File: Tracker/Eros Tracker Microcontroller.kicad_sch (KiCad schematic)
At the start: 20 parts, among them M1 Motor_DC, Q1 NX138BKSX, Q2 NX138BKSX, Q3 DMP31D7LDW-7, SW1 EVQ-P7A01P, U1 ESP32-C3-WROOM-02-N4

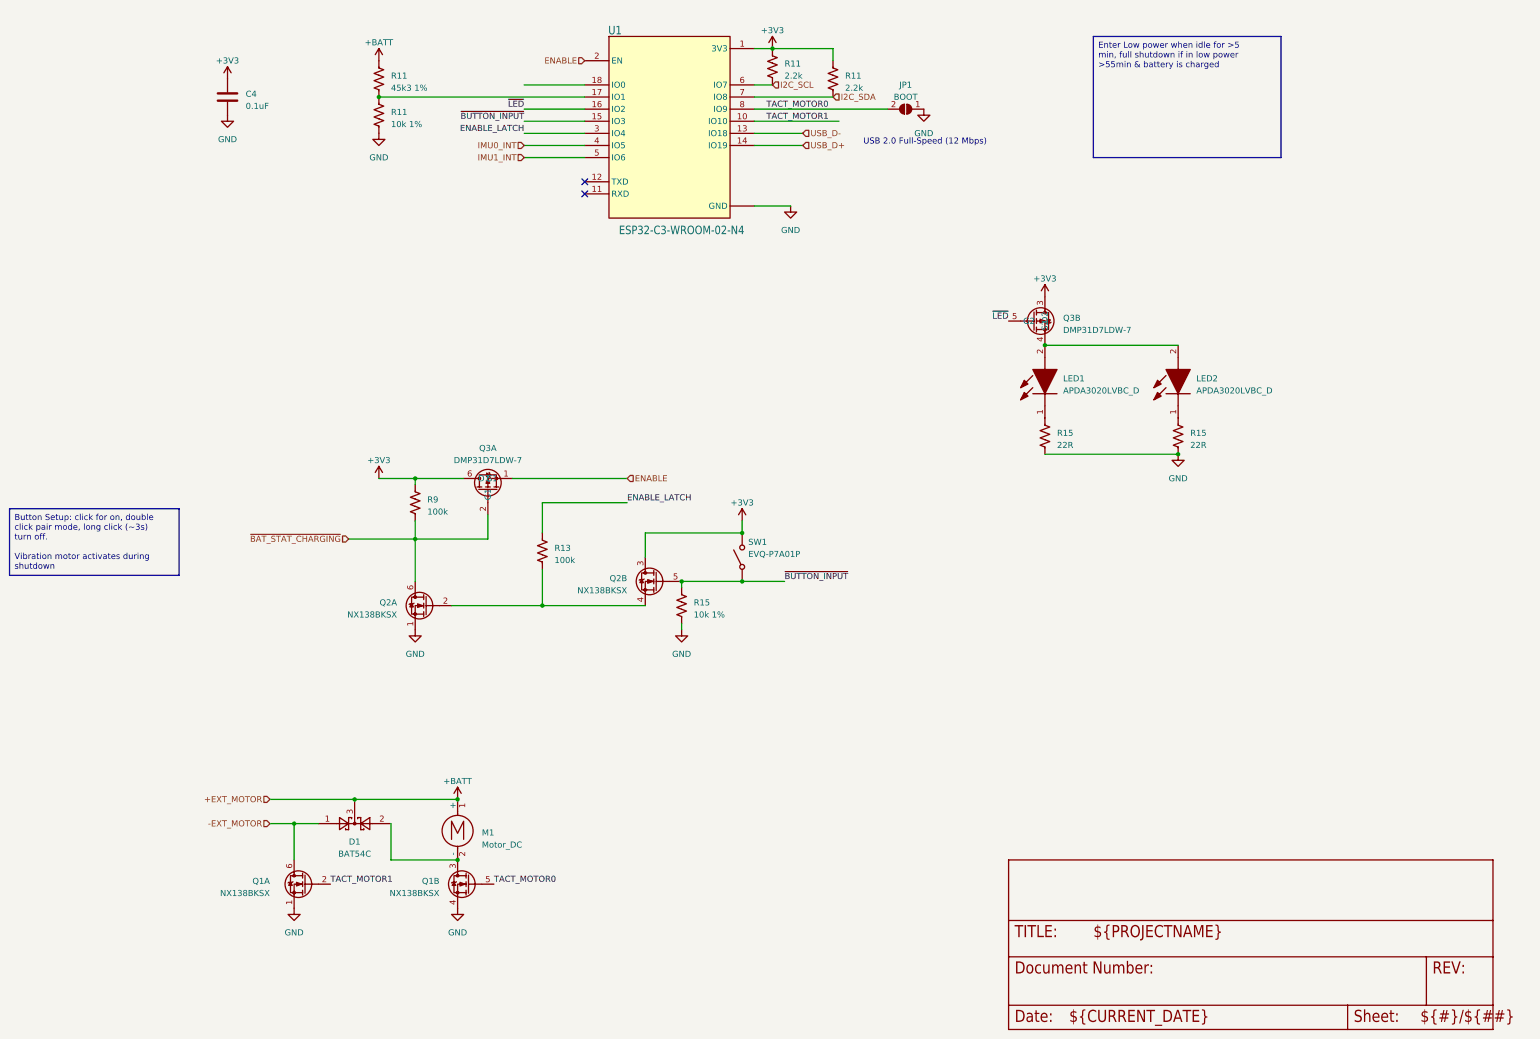
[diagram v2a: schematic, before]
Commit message: RevC release. Power passthrough, battery voltage monitoring, IMU interrupt line fixed. TVS diodes added to all human-reachable connections.
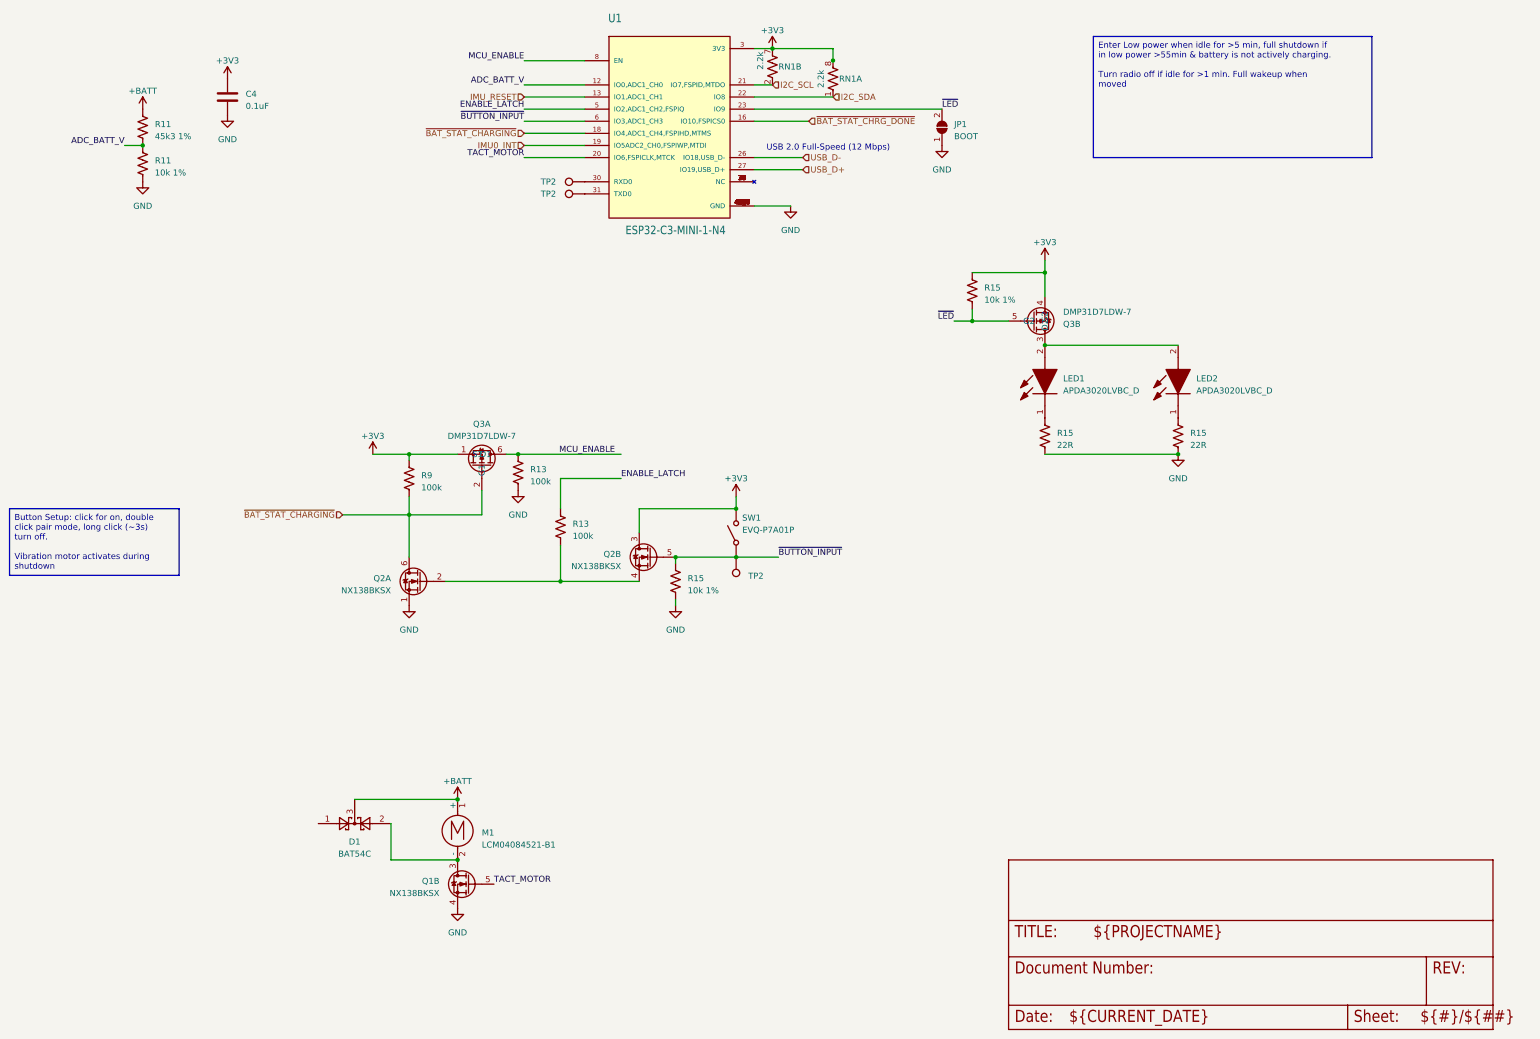
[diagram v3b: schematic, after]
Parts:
- removed unit 1 of Q1
- removed R11 (x2): 2.2k, Resistor_SMD:R_0805_2012Metric, symbol Device:R_US
- added R13: 100k, Resistor_SMD:R_0402_1005Metric, symbol Device:R_US
- added R15: 10k 1%, Resistor_SMD:R_0402_1005Metric, symbol Device:R_US
- added RN1: 2.2k, Eros Tracker:CAY10-xxxJ4, symbol Eros Tracker:CAY10-xxxJ4
- added TP2 (x3): TestPoint, TestPoint:TestPoint_Pad_D1.0mm, symbol Connector:TestPoint
- C4: footprint Capacitor_SMD:C_0805_2012Metric -> Capacitor_SMD:C_0402_1005Metric; Manufacturer_Part_Number CL21B104MACNNNC -> CL05B104KA5NNNC; Mouser Part Number 187-CL21B104MACNNNC -> 187-CL05B104KA5NNNC; Mouser Price/Stock https://www.mouser.com/ProductDetail/Samsung-Electro-Mechanics/CL21B104MACNNNC?qs=xZ%2FP%252Ba9zWqbIolF6La19LA%3D%3D -> https://www.mouser.com/ProductDetail/Samsung-Electro-Mechanics/CL05B104KA5NNNC?qs=Efv9o2T6U88DLyyMSzjXSQ%3D%3D
- LED1, LED2: footprint APDA3020LVBCD -> Eros Tracker:APDA3020LVBCD
- M1: value Motor_DC -> LCM04084521-B1; footprint Jumper:SolderJumper-2_P1.3mm_Open_RoundedPad1.0x1.5mm -> Eros Tracker:LCM04084521-B1
- Q3: footprint SOT65P210X110-6N -> Eros Tracker:SOT65P210X110-6N
- R11, R15: footprint Resistor_SMD:R_0805_2012Metric -> Resistor_SMD:R_0402_1005Metric; Manufacturer_Part_Number RT0805FRE0710KL -> RT0402FRE0710KL; Mouser Part Number 603-RT0805FRE0710KL -> 603-RT0402FRE0710KL; Mouser Price/Stock https://www.mouser.com/ProductDetail/YAGEO/RT0805FRE0710KL?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 -> https://www.mouser.com/ProductDetail/YAGEO/RT0402FRE0710KL?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
- R11: footprint Resistor_SMD:R_0805_2012Metric -> Resistor_SMD:R_0402_1005Metric; Manufacturer_Name YAGEO -> Susumu; Manufacturer_Part_Number RT0805DRE0745K3L -> RR0510P-4532-D; Mouser Part Number 603-RT0805DRE0745K3L -> 754-RR0510P-4532D; Mouser Price/Stock https://www.mouser.com/ProductDetail/YAGEO/RT0805DRE0745K3L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 -> https://www.mouser.com/ProductDetail/Susumu/RR0510P-4532-D?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
- R13, R9: footprint Resistor_SMD:R_0805_2012Metric -> Resistor_SMD:R_0402_1005Metric; Manufacturer_Part_Number RT0805FRE07100KL -> RT0402FRE07100KL; Mouser Part Number 603-RT0805FRE07100KL -> 603-RT0402FRE07100KL; Mouser Price/Stock https://www.mouser.com/ProductDetail/YAGEO/RT0805FRE07100KL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 -> https://www.mouser.com/ProductDetail/YAGEO/RT0402FRE07100KL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
- R15: footprint Resistor_SMD:R_0805_2012Metric -> Resistor_SMD:R_0402_1005Metric; Manufacturer_Part_Number RT0805FRE0722RL -> RT0402FRE0722RL; Mouser Part Number 603-RT0805FRE0722RL -> 603-RT0402FRE0722RL; Mouser Price/Stock https://www.mouser.com/ProductDetail/YAGEO/RT0805FRE0722RL?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 -> https://www.mouser.com/ProductDetail/YAGEO/RT0402FRE0722RL?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
- SW1: footprint EVQP7J01P -> Eros Tracker:EVQ-P7J01P
- U1: value ESP32-C3-WROOM-02-N4 -> ESP32-C3-MINI-1-N4; footprint Eros Tracker:MODULE_ESP32-C3-WROOM-02-H4 -> Eros Tracker:XCVR_ESP32-C3-MINI-1-N4; symbol Eros Tracker:ESP32-C3-WROOM-02-N4 -> Eros Tracker:ESP32-C3-MINI-1-N4; MANUFACTURER (none) -> Espressif Systems; MAXIMUM_PACKAGE_HEIGHT (none) -> 2.55mm; Manufacturer_Part_Number ESP32-C3-WROOM-02-N4 -> ESP32-C3-MINI-1-N4; Mouser Part Number 356-ESP32C3WROOM02N4 -> 356-ESP32-C3-MINI1N4; Mouser Price/Stock https://www.mouser.com/ProductDetail/Espressif-Systems/ESP32-C3-WROOM-02-N4?qs=sGAEpiMZZMu3sxpa5v1qrhrB%252BBlYHY1O2YkhFjq1w70%3D -> https://www.mouser.com/ProductDetail/Espressif-Systems/ESP32-C3-MINI-1-N4?qs=stqOd1AaK7%252B%2FpH3qqyGehA%3D%3D; PARTREV (none) -> v1.0; STANDARD (none) -> Manufacturer Recommendations
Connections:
- net IMU1_INT is gone; now on net ENABLE_LATCH: U1.5 (IO2,ADC1_CH2,FSPIQ)
- net +3V3: now also Q3.1 (S1), Q3.4 (S2), U1.3 (3V3), R15.1, RN1.7, RN1.8; no longer Q3.3 (D2), Q3.6 (D1), U1.1 (3V3)
- net ENABLE_LATCH: no longer U1.3 (IO4)
- net GND: now also U1.1 (GND), U1.11 (GND), U1.14 (GND), U1.2 (GND), U1.40 (GND), U1.41 (GND), U1.42 (GND), U1.43 (GND), U1.44 (GND), U1.45 (GND), U1.46 (GND), U1.47 (GND), U1.48 (GND), U1.49_1 (GND), U1.49_2 (GND), U1.49_3 (GND), U1.49_4 (GND), U1.49_5 (GND), U1.49_6 (GND), U1.49_7 (GND), U1.49_8 (GND), U1.49_9 (GND), U1.50 (GND), U1.51 (GND), U1.52 (GND), U1.53 (GND), R13.2; no longer U1.19 (GND), U1.20 (GND), U1.21 (GND), U1.22 (GND), U1.23 (GND), U1.24 (GND), U1.25 (GND), U1.26 (GND), U1.27 (GND), U1.28 (GND), U1.29 (GND), U1.30 (GND), U1.31 (GND), U1.32 (GND), U1.33 (GND), U1.34 (GND), U1.35 (GND), U1.9 (GND)
- net I2C_SCL: now also U1.21 (IO7,FSPID,MTDO), RN1.2; no longer U1.6 (IO7)
- net I2C_SDA: now also U1.22 (IO8), RN1.1; no longer U1.7 (IO8)
- net IMU0_INT: now also U1.19 (IO5ADC2_CH0,FSPIWP,MTDI); no longer U1.4 (IO5)
- net USB_D+: now also U1.27 (IO19,USB_D+); no longer U1.14 (IO19)
- net USB_D-: now also U1.26 (IO18,USB_D-); no longer U1.13 (IO18)
- net ~{BAT_STAT_CHARGING}: now also U1.18 (IO4,ADC1_CH4,FSPIHD,MTMS)
- net ~{BUTTON_INPUT}: now also U1.6 (IO3,ADC1_CH3), TP2.1; no longer U1.15 (IO3)
- net ~{LED}: now also JP1.2 (B), U1.23 (IO9), R15.2; no longer U1.16 (IO2)
- net at LED1.2 (A), LED2.2 (A): now also Q3.3 (D2); no longer Q3.4 (S2)
- net ADC_BATT_V: now reaches R11.1, R11.2
- net ADC_BATT_V: now also U1.12 (IO0,ADC1_CH0); no longer U1.17 (IO1)
- net -EXT_MOTOR: no longer names the net of D1.1
- removed net ENABLE: Q3.1 (S1), U1.2 (EN)
- removed net TACT_MOTOR0: JP1.2 (B), Q1.5 (G2), U1.8 (IO9)
- net TACT_MOTOR1: no longer names the net of U1.10 (NC)
- net TACT_MOTOR1: now also U1.15 (NC), U1.17 (NC), U1.24 (NC), U1.25 (NC), U1.28 (NC), U1.29 (NC), U1.32 (NC), U1.33 (NC), U1.34 (NC), U1.35 (NC), U1.4 (NC), U1.7 (NC), U1.9 (NC)
- new net: TP2.1, U1.31 (TXD0)
- new net: TP2.1, U1.30 (RXD0)
- new net IMU_RESET: U1.13 (IO1,ADC1_CH1)
- new net MCU_ENABLE: Q3.6 (D1), R13.1, U1.8 (EN)
- new net TACT_MOTOR: Q1.5 (G2), U1.20 (IO6,FSPICLK,MTCK)
- new net ~{BAT_STAT_CHRG_DONE}: U1.16 (IO10,FSPICS0)
- no-connect marks 2 -> 0
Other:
- moved on the sheet: JP1, Q2A, Q2B, Q3A, R11, R13, R15, R9, SW1
